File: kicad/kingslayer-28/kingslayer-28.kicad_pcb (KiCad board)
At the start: 2 copper layers, 123 parts, among them IC1 STM32F303CCT7, IC2 IS31FL3731-QFLS2-TR, IC3 LM3940IMP-3.3_NOPB, J1 Conn_01x04_Pin, K1 KEYSW, K10 KEYSW, K11 KEYSW, K12 KEYSW, K13 KEYSW, K14 KEYSW, K15 KEYSW, K16 KEYSW, K17 KEYSW, K18 KEYSW, K19 KEYSW, K2 KEYSW, K20 KEYSW, K21 KEYSW, K22 KEYSW, K23 KEYSW, K24 KEYSW, K25 KEYSW, K26 KEYSW, K27 KEYSW, K28 KEYSW, K3 KEYSW, K4 KEYSW, K5 KEYSW, K6 KEYSW, K7 KEYSW, K8 KEYSW, K9 KEYSW, SW1 SS12D07, X1 IC21008.000M30.0EE1B

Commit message: placed switches, switch diodes and mounting holes
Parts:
- D1, D10, D11, D12, D13, D14, D15, D16, D17, D18, D19, D2, D20, D21, D22, D23, D24, D25, D26, D27, D28, D3, D4, D5, D6, D7, D8, D9: moved to B.Cu
- D29, D30, D31, D32, D33, D34, D35, D36, D37, D38, D39, D40, D41, D42, D43, D44, D45, D46, D47, D48, D49, D50, D51, D52, D53, D54, D55, D56: moved to F.Cu
- moved R7 250.6 mm to (238.7, 82.5) (x2)
- moved R8 250.6 mm to (238.7, 85.5) (x2)
- moved K7 200.8 mm to (203.5, 54.8)
- moved K6 178.7 mm to (184.5, 54.8)
- moved K5 157.5 mm to (165.5, 54.8)
- moved K23 155.0 mm to (189.4, 111.8)
- moved K22 150.5 mm to (170.4, 111.8)
- moved K12 148.5 mm to (175.1, 73.8)
- moved R8 148.2 mm to (244.2, 85.5)
- moved R7 148.2 mm to (244.2, 82.4)
- moved C1 147.9 mm to (239.4, 99.2)
- moved C10 147.9 mm to (224.9, 72.2)
- moved C11 147.9 mm to (234.9, 99.2)
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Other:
- board outline added: 133 x 95 mm

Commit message: initial placement
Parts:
- removed the R7 at (238.7, 82.5)
- removed the R7 at (244.2, 82.4)
- removed the R8 at (238.7, 85.5)
- removed the R8 at (244.2, 85.5)
- moved R6 64.5 mm to (186.9, 77.2), turned to 90 degrees
- moved C9 58.8 mm to (185.4, 82.9), turned to -90 degrees
- moved C12 57.7 mm to (187.0, 65.3), turned to 180 degrees
- moved C8 56.1 mm to (193.5, 88.7)
- moved R2 56.0 mm to (189.8, 88.6)
- moved R1 54.2 mm to (194.3, 80.3)
- moved F1 50.6 mm to (207.6, 64.2), turned to 180 degrees
- moved IC2 50.5 mm to (190.9, 84.6)
- moved R3 48.3 mm to (189.6, 78.0), turned to -90 degrees
- moved R9 44.9 mm to (201.2, 74.2)
- moved C11 43.6 mm to (201.5, 71.0), turned to 180 degrees
- moved C1 41.7 mm to (198.5, 91.4), turned to 180 degrees
- moved BOOT0 40.5 mm to (187.6, 71.1)
- moved C3 39.4 mm to (197.5, 89.2), turned to 180 degrees
- moved J1 37.9 mm to (194.6, 76.0), turned to 180 degrees
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- renumbered SW1 to BOOT0, S1 to RESET
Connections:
- BOOT0 pad 1: +5V -> GND
- BOOT0 pad 3: +5V -> +3V3
- C1 pad 2: +5V -> GND
- C10 pad 1: +5V -> GND
- C11 pad 2: +5V -> GND
- C12 pad 1: +5V -> +3V3
- C12 pad 2: +5V -> GND
- C2 pad 2: +5V -> GND
- C3 pad 1: +5V -> +3V3
- C3 pad 2: +5V -> GND
- C4 pad 1: +5V -> +3V3
- C4 pad 2: +5V -> GND
- C5 pad 1: +5V -> +3V3
- C5 pad 2: +5V -> GND
- C6 pad 1: +5V -> +3V3
- C6 pad 2: +5V -> GND
- C7 pad 1: +5V -> +3V3
- C7 pad 2: +5V -> GND
- C8 pad 2: +5V -> GND
- C9 pad 2: +5V -> GND
- IC1 pad 1: +5V -> +3V3
- IC1 pad 23: +5V -> GND
- IC1 pad 24: +5V -> +3V3
- IC1 pad 35: +5V -> GND
- IC1 pad 36: +5V -> +3V3
- IC1 pad 47: +5V -> GND
- IC1 pad 48: +5V -> +3V3
- IC1 pad 8: +5V -> GND
- IC1 pad 9: +5V -> +3V3
- IC2 pad 18: +5V -> GND
- IC2 pad 29: +5V -> GND
- IC2 pad 5: +5V -> GND
- IC3 pad 2: +5V -> GND
- IC3 pad 3: +5V -> +3V3
- IC3 pad 4: +5V -> GND
- J1 pad 1: +5V -> GND
- J1 pad 4: +5V -> +3V3
- R2 pad 2: +5V -> GND
- R3 pad 1: +5V -> +3V3
- R4 pad 1: +5V -> +3V3
- R5 pad 1: +5V -> +3V3
- R6 pad 2: +5V -> GND
- R7 pad 2: +5V -> GND
- R8 pad 2: +5V -> GND
- R9 pad 1: +5V -> +3V3
- RESET pad 1: +5V -> GND
- RESET pad 3: +5V -> GND
- USB1 pad A1: +5V -> GND
- USB1 pad A12: +5V -> GND
- USB1 pad B1: +5V -> GND
- USB1 pad B12: +5V -> GND
- USB1 pad S1: +5V -> GND

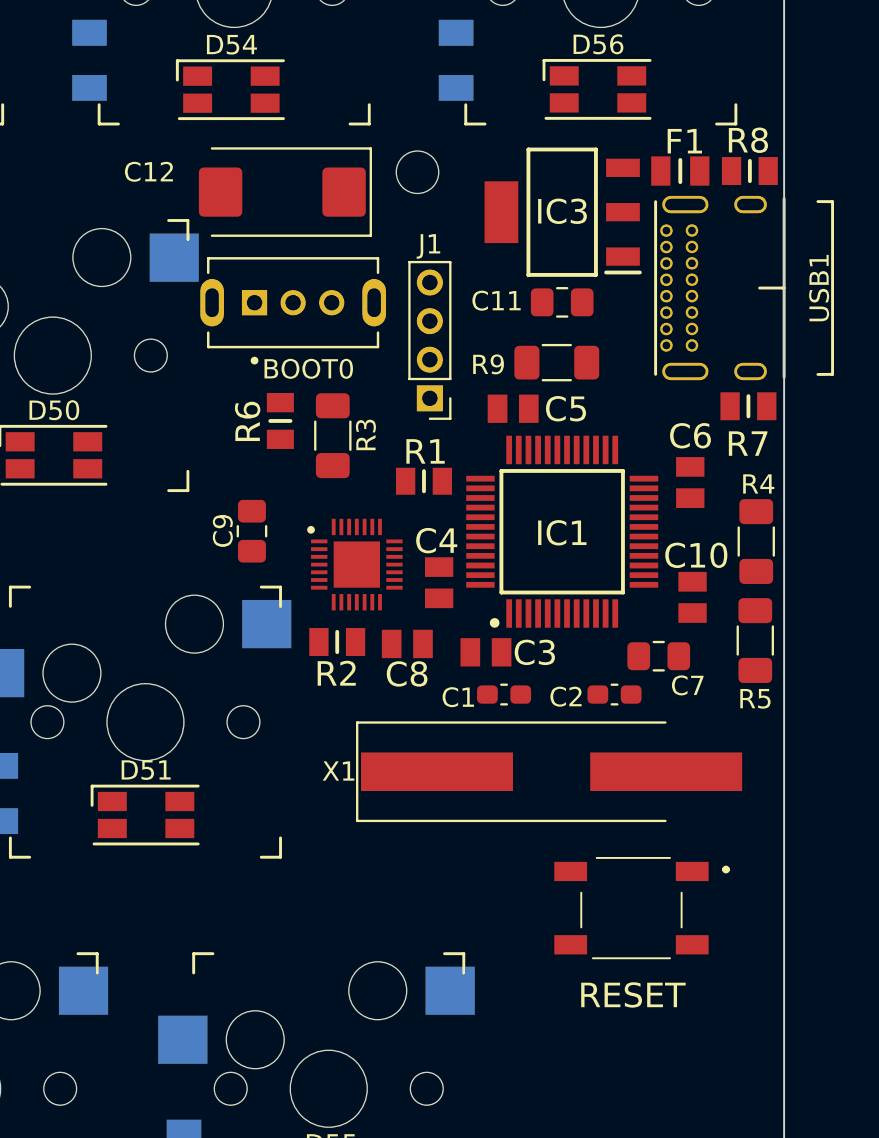
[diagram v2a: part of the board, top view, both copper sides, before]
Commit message: swap mcu location
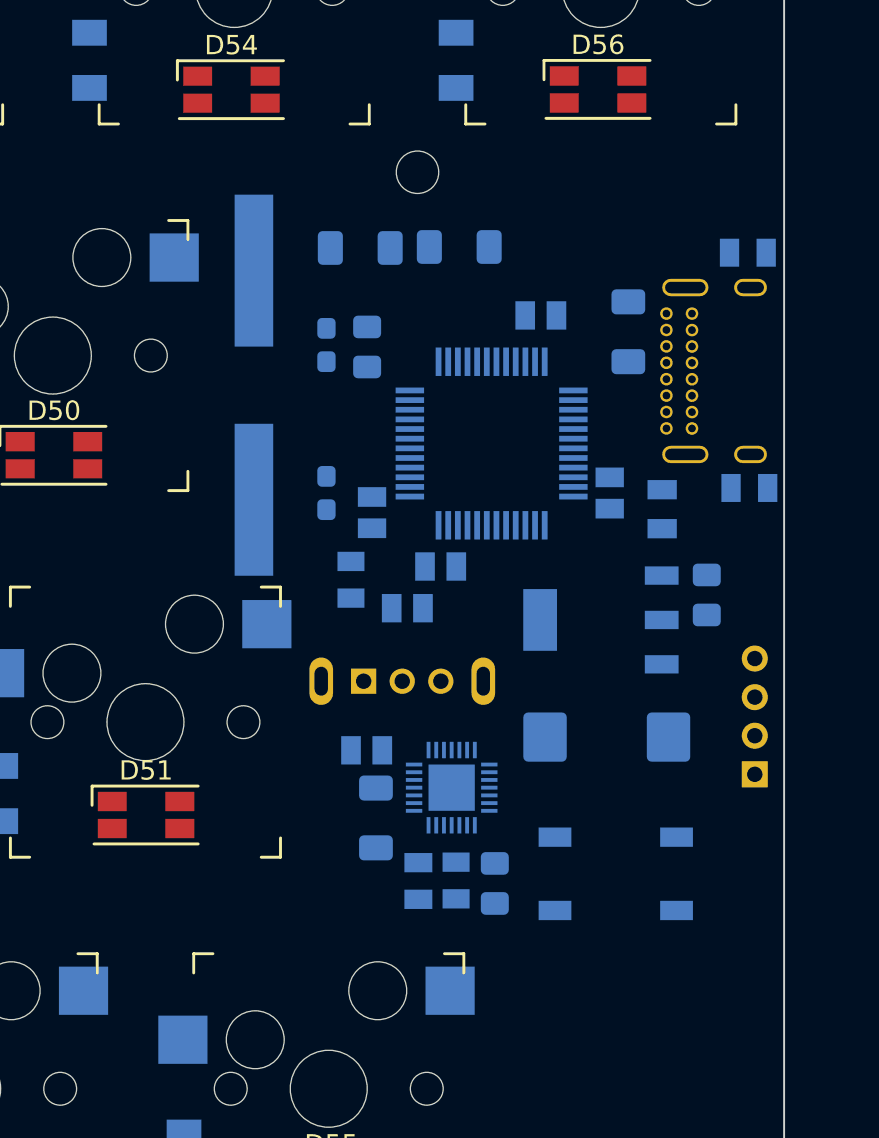
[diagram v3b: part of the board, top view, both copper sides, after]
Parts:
- C1, C10, C11, C12, C2, C3, C4, C5, C6, C7, C8, C9, F1, IC1, IC2, IC3, J1, R1, R2, R3, R4, R5, R6, R7, R8, R9, USB1, X1: moved to B.Cu
- S1: renamed from RESET; moved to B.Cu
- SW1: renamed from BOOT0; moved to B.Cu
- moved C12 32.9 mm to (203.8, 93.6)
- moved R5 28.9 mm to (191.0, 68.2), turned to 0 degrees
- moved J1 25.8 mm to (211.5, 95.5), turned to 0 degrees
- moved R6 25.5 mm to (196.0, 101.0), turned to -90 degrees
- moved X1 25.3 mm to (185.5, 75.3), turned to 90 degrees
- moved C2 23.5 mm to (189.3, 73.3), turned to 90 degrees
- moved C9 22.2 mm to (198.0, 101.2)
- moved C7 22.0 mm to (191.4, 73.4), turned to 90 degrees
- moved R4 21.7 mm to (196.2, 68.2), turned to 0 degrees
- moved IC3 21.2 mm to (203.5, 87.5)
- moved SW1 20.4 mm to (193.2, 90.7)
- moved R3 19.9 mm to (191.8, 97.8)
- moved F1 17.6 mm to (206.7, 81.8), turned to -90 degrees
- moved C11 16.9 mm to (209.0, 86.2), turned to -90 degrees
- moved R8 16.4 mm to (211.2, 80.7)
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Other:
- board text added: "BOOT0"
- board text added: "RESET"

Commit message: routing in progress
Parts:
- moved C7 8.81 mm to (191.4, 82.2), turned to -90 degrees
- moved C3 5.08 mm to (191.4, 76.9)
- moved R9 4.84 mm to (204.3, 77.4)
- moved R7 3.92 mm to (207.2, 68.3)
- moved R3 3.83 mm to (190.9, 101.5), turned to 0 degrees
- moved R2 3.25 mm to (191.4, 99.2), turned to 180 degrees
- moved C2 2.35 mm to (189.1, 75.6), turned to -90 degrees
- moved C1 1.94 mm to (189.1, 79.0), turned to 90 degrees
- moved C8 1.85 mm to (189.5, 94.3)
- moved R6 1.03 mm to (196.0, 102.0)
- moved R1 0.97 mm to (190.2, 86.3)
- moved R8 0.90 mm to (210.4, 81.1), turned to 180 degrees
- moved C10 0.60 mm to (192.9, 87.2), turned to 0 degrees
- moved C4 0.56 mm to (194.6, 84.7)
- moved C5 0.49 mm to (204.0, 81.4)
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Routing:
- net GND: track 0.00 -> 100.6 mm, vias 0 -> 13
- net +3V3: track 0.00 -> 78.5 mm
- net nrst: track 0.00 -> 39.7 mm, vias 0 -> 2
- net /RGB/scl: track 0.00 -> 28.7 mm, vias 0 -> 2
- net /RGB/sda: track 0.00 -> 27.8 mm, vias 0 -> 2
- net swdio: track 0.00 -> 25.6 mm
- net swclk: track 0.00 -> 22.4 mm
- net xtal2: track 0.00 -> 15.7 mm
- net boot0: track 0.00 -> 15.2 mm, vias 0 -> 4
- net Net-(F1-Pad1): track 0.00 -> 15.1 mm, vias 0 -> 2
- net d+: track 0.00 -> 11.1 mm, vias 0 -> 2
- net d-: track 0.00 -> 9.41 mm
- net xtal1: track 0.00 -> 9.15 mm
- net Net-(USB1-CC2): track 0.00 -> 8.43 mm
- net +5V: track 0.00 -> 7.70 mm
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- added copper zone on B.Cu, net GND

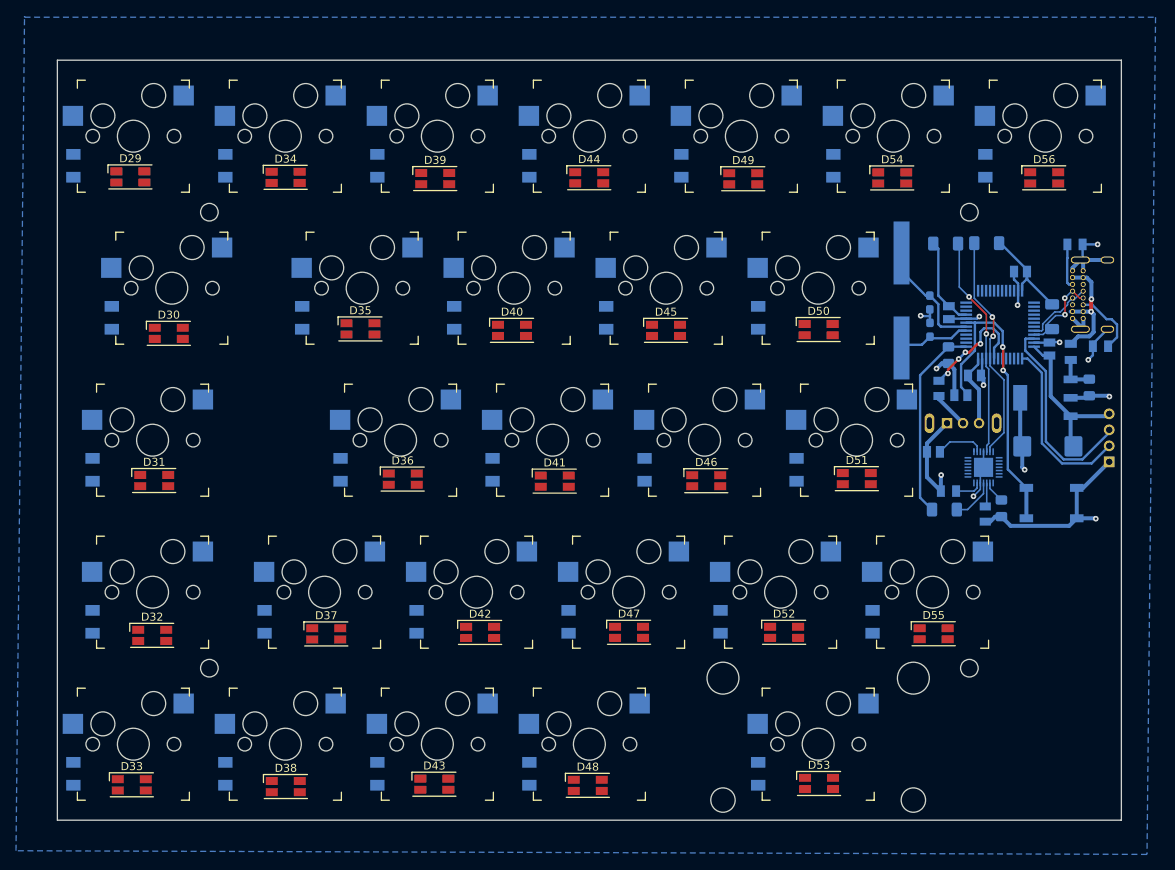
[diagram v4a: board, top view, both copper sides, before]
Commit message: revert footprints, finalize placement
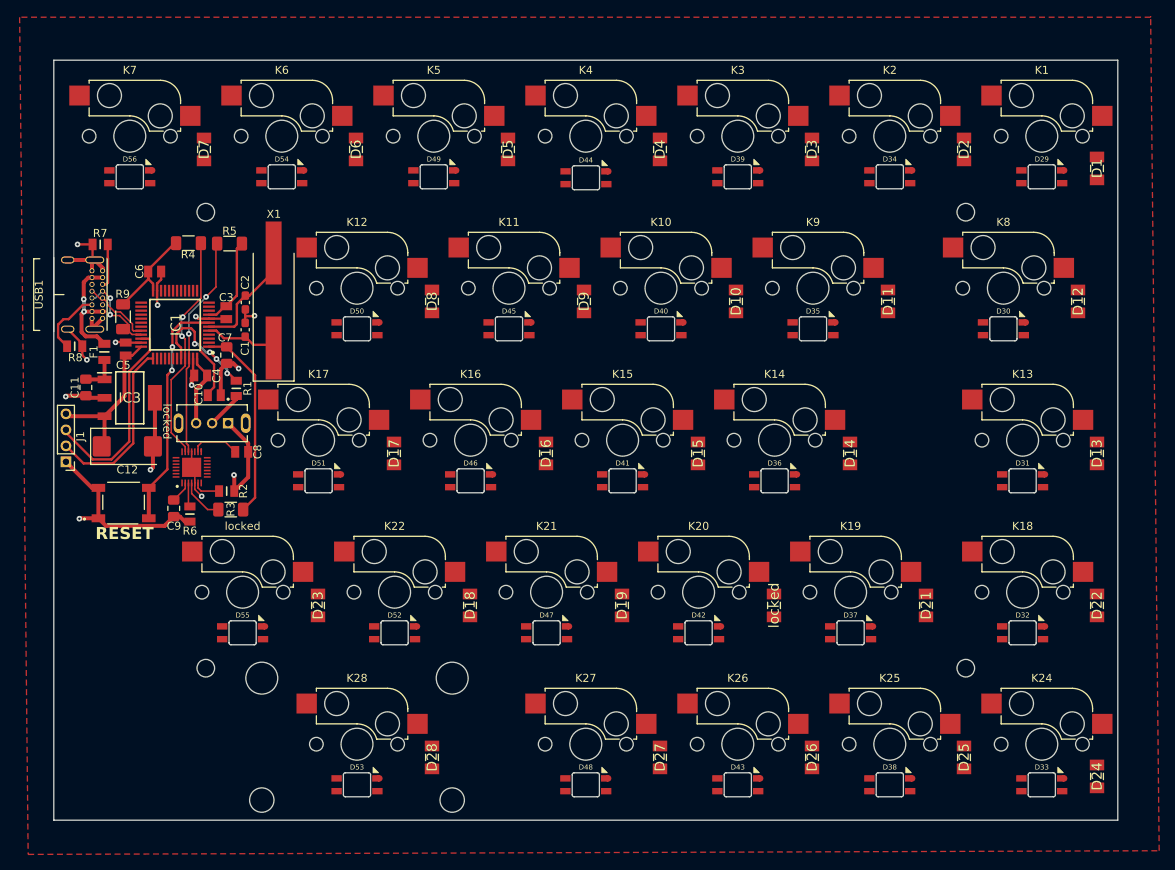
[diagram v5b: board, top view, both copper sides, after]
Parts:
- C1, C10, C11, C12, C2, C3, C4, C5, C6, C7, C8, C9, D1, D10, D11, D12, D13, D14, D15, D16, D17, D18, D19, D2, D21, D22, D23, D24, D25, D26, D27, D28, D3, D4, D5, D6, D7, D8, D9, F1, IC1, IC2, IC3, J1, R1, R2, R3, R4, R5, R6, R7, R8, R9, S1, SW1, USB1, X1: moved to F.Cu
- D29, D30, D31, D32, D33, D34, D35, D36, D37, D38, D39, D40, D41, D42, D43, D44, D45, D46, D47, D48, D49, D50, D51, D52, D53, D54, D55, D56: footprint LED_SMD:LED_RGB_1210 -> acheron_Components:LED_RGB_SMD_6028_2.8x3.5mm_Square
- H1, H2, H3, H4, H5, K1, K10, K11, K12, K13, K14, K15, K16, K17, K18, K19, K2, K20, K21, K22, K24, K25, K26, K27, K28, K3, K4, K5, K6, K7, K8, K9: moved to B.Cu
- locked: renamed from D20; moved to F.Cu
- locked: renamed from K23; moved to B.Cu
- moved USB1 133.4 mm to (79.6, 74.6)
- moved J1 130.4 mm to (81.1, 95.5), turned to 180 degrees
- moved R8 128.2 mm to (82.2, 81.1), turned to 0 degrees
- moved D1 128.0 mm to (210.0, 58.8)
- moved D24 128.0 mm to (210.0, 134.8)
- moved D13 125.6 mm to (210.0, 94.5)
- moved D22 125.6 mm to (210.0, 113.5)
- moved C11 125.4 mm to (83.6, 86.2)
- moved R7 121.9 mm to (85.3, 68.3), turned to 180 degrees
- moved F1 120.8 mm to (85.9, 81.8)
- moved D12 120.8 mm to (207.6, 75.5)
- moved R9 116.1 mm to (88.2, 77.4)
- moved S1 116.0 mm to (88.3, 100.7), turned to 0 degrees
- moved C5 115.5 mm to (88.5, 81.4)
- moved C12 115.1 mm to (88.7, 93.6), turned to 0 degrees
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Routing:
- added copper zone on F.Cu, net GND
- removed copper zone on B.Cu, net GND
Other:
- board text added: "locked"
- board text removed: "BOOT0"

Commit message: backup
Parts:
- moved R6 11.3 mm to (105.5, 95.0), turned to 90 degrees
- moved C8 9.98 mm to (98.9, 103.3)
- moved C9 9.13 mm to (99.7, 93.8), turned to 0 degrees
- moved R3 8.28 mm to (95.7, 95.7), turned to -90 degrees
- moved R2 4.72 mm to (103.4, 95.0), turned to 90 degrees
- moved IC2 4.64 mm to (100.0, 99.5), turned to -90 degrees
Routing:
- net col0: track 0.00 -> 197.2 mm, vias 0 -> 7
- net row4: track 0.00 -> 180.5 mm, vias 0 -> 2
- net cb6: track 0.00 -> 176.9 mm, vias 0 -> 2
- net col1: track 0.00 -> 174.0 mm, vias 0 -> 7
- net col2: track 0.00 -> 160.4 mm, vias 0 -> 7
- net ca3: track 0.00 -> 157.6 mm, vias 0 -> 2
- net row3: track 0.00 -> 152.2 mm, vias 0 -> 2
- net col3: track 0.00 -> 143.1 mm, vias 0 -> 6
- net row0: track 0.00 -> 141.5 mm, vias 0 -> 2
- net cb1: track 0.00 -> 140.5 mm, vias 0 -> 5
- net cb3: track 0.00 -> 137.4 mm, vias 0 -> 2
- net col4: track 0.00 -> 128.3 mm, vias 0 -> 6
- net cb7: track 0.00 -> 118.4 mm, vias 0 -> 3
- net ca6: track 0.00 -> 113.4 mm, vias 0 -> 2
- net ca9: track 0.00 -> 111.7 mm
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
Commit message: finish routing?
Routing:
- net ca2: track 79.8 -> 249.3 mm, vias 2 -> 14
- net ca1: track 108.5 -> 272.2 mm, vias 0 -> 10
- net ca8: track 9.53 -> 170.8 mm, vias 1 -> 14
- net ca4: track 39.8 -> 195.0 mm, vias 2 -> 15
- net ca5: track 22.1 -> 176.8 mm, vias 2 -> 14
- net ca7: track 11.0 -> 156.4 mm, vias 0 -> 12
- net cb2: track 53.2 -> 180.8 mm, vias 4 -> 15
- net cb1: track 140.5 -> 252.7 mm, vias 5 -> 15
- net cb5: track 84.3 -> 174.1 mm, vias 3 -> 7
- net cb4: track 86.0 -> 174.5 mm, vias 3 -> 7
- net row2: track 36.4 -> 124.3 mm, vias 2 -> 6
- net row1: track 49.0 -> 130.2 mm
- net ca3: track 157.6 -> 210.2 mm, vias 2 -> 4
- net ca9: track 111.7 -> 155.8 mm, vias 0 -> 4
- net cb7: track 118.4 -> 153.7 mm, vias 3 -> 5
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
